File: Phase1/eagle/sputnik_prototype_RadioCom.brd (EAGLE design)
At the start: 100 x 80 mm, 74 parts, among them X2 332-22, Y1 32MHz

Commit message: fixed symbols
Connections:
- net N$20 renamed LNA_OUT
- net N$5 renamed LNA_IN
- removed net N$2 (its old number): C24.1, C43.+, L8.2, R1.2
- removed net N$9: C36.1, U$7.5
- new net VBIAS: C24.1, C36.1, C43.+, L8.2, R1.2, U$7.5

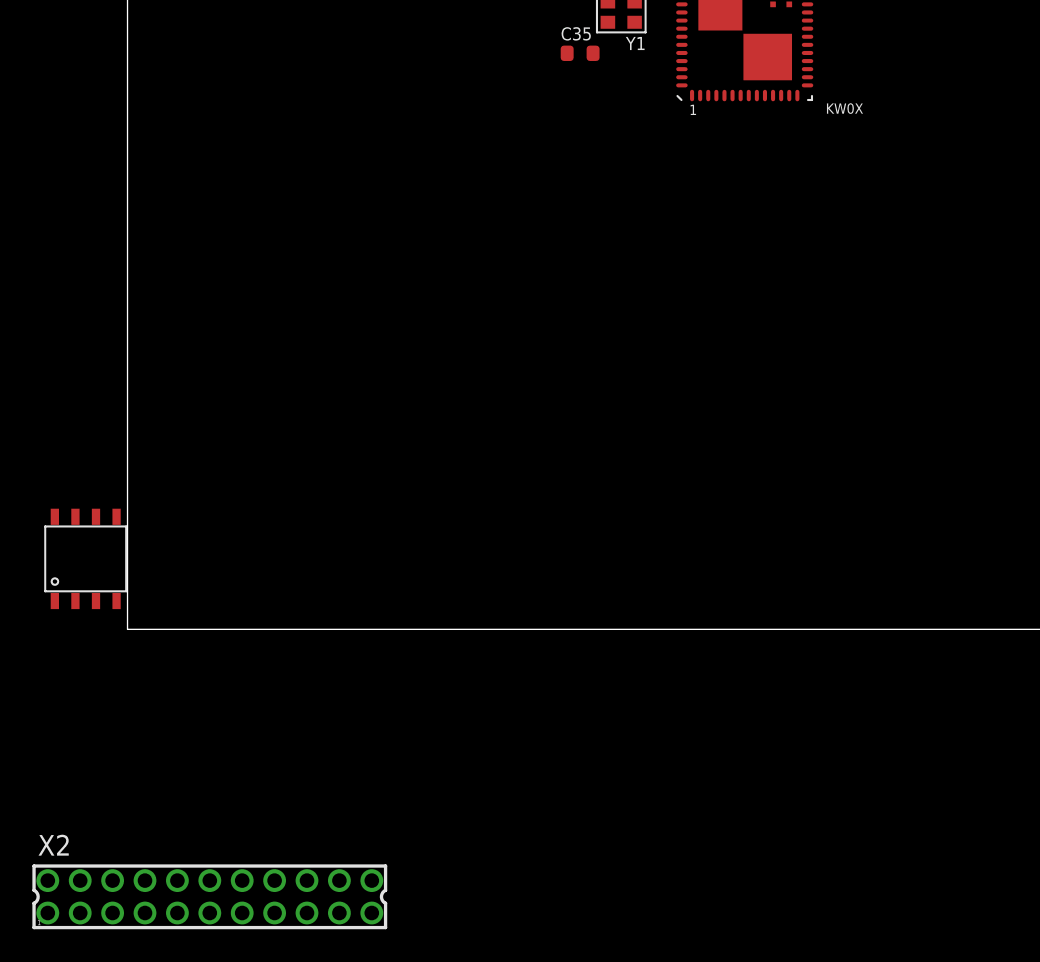
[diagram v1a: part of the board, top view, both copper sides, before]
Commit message: Added GPIO bus
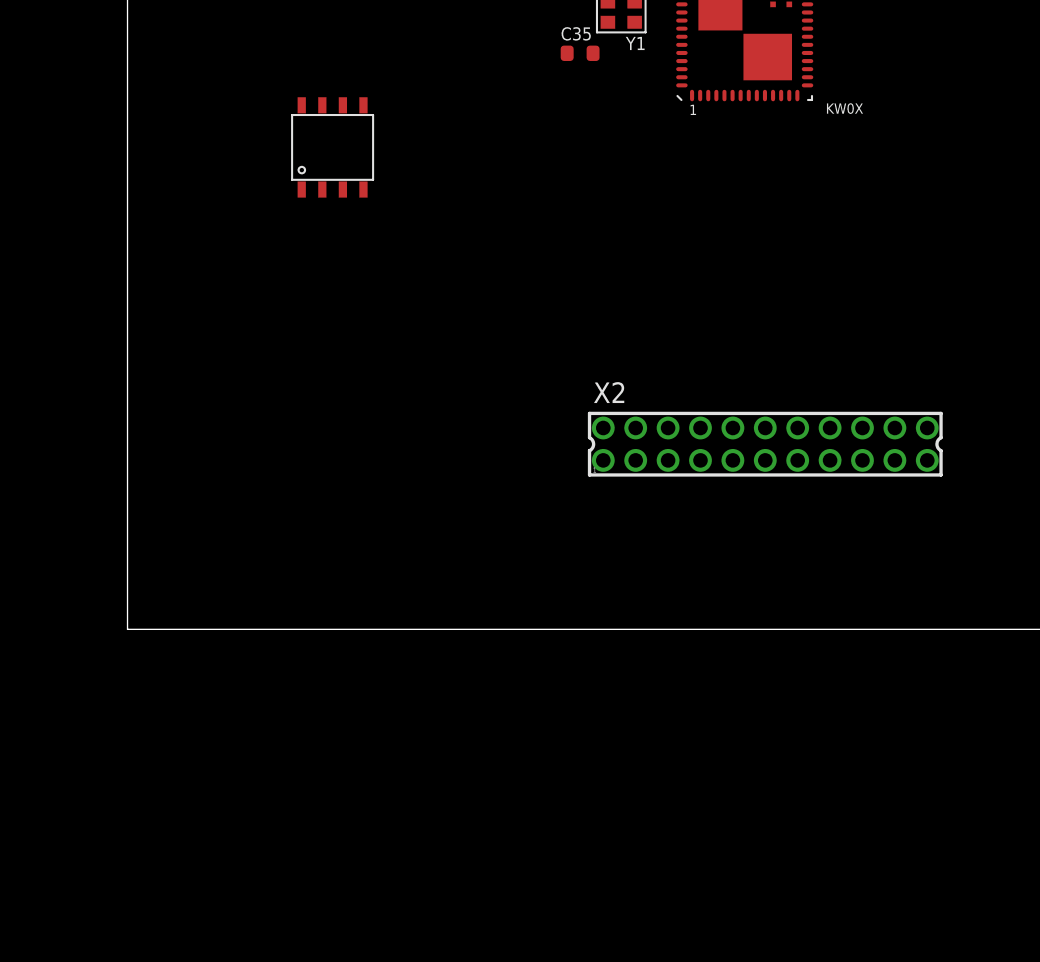
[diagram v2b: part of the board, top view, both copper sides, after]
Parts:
- moved X2 44.2 mm to (39.4, 11.4)
- moved U$1 29.6 mm to (10.2, 31.8)
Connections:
- removed net N$32: KW0X.50, X2.2
- removed net N$33: KW0X.5, X2.3
- removed net N$35: KW0X.6, X2.4
- removed net N$36: KW0X.7, X2.5
- removed net N$37: KW0X.8, X2.6
- removed net N$38: KW0X.9, X2.7
- removed net N$4: KW0X.49, X2.1
- removed net PTB0: KW0X.17
- removed net PTB1: KW0X.18, X2.12
- removed net PTB17: KW0X.22, X2.14
- removed net PTB2: KW0X.21, X2.13
- removed net PTBO: X2.11
- removed net PTC1: KW0X.24, X2.15
- removed net PTC2: KW0X.25, X2.16
- removed net PTC3: KW0X.26, X2.17
- removed net PTC4: KW0X.23, X2.18
- removed net PTC5: KW0X.59, X2.19
- removed net PTC6: KW0X.60, X2.20
- new net GPIO0: KW0X.17, X2.1
- new net GPIO1: KW0X.18, X2.2
- new net GPIO10: KW0X.49, X2.11
- new net GPIO11: KW0X.50, X2.12
- new net GPIO12: KW0X.5, X2.13
- new net GPIO13: KW0X.6, X2.14
- new net GPIO14: KW0X.7, X2.15
- new net GPIO15: KW0X.8, X2.16
- new net GPIO16: KW0X.9, X2.17
- new net GPIO2: KW0X.21, X2.3
- new net GPIO3: KW0X.22, X2.4
- new net GPIO4: KW0X.24, X2.5
- new net GPIO5: KW0X.25, X2.6
- new net GPIO6: KW0X.26, X2.7
- new net GPIO7: KW0X.23, X2.8
- new net GPIO8: KW0X.59, X2.9
- new net GPIO9: KW0X.60, X2.10
- net PE0/UART0RX: now also X2.18; no longer X2.8
- net PE1/UART0TX: now also X2.19; no longer X2.9
- net PE3: now also X2.20; no longer X2.10

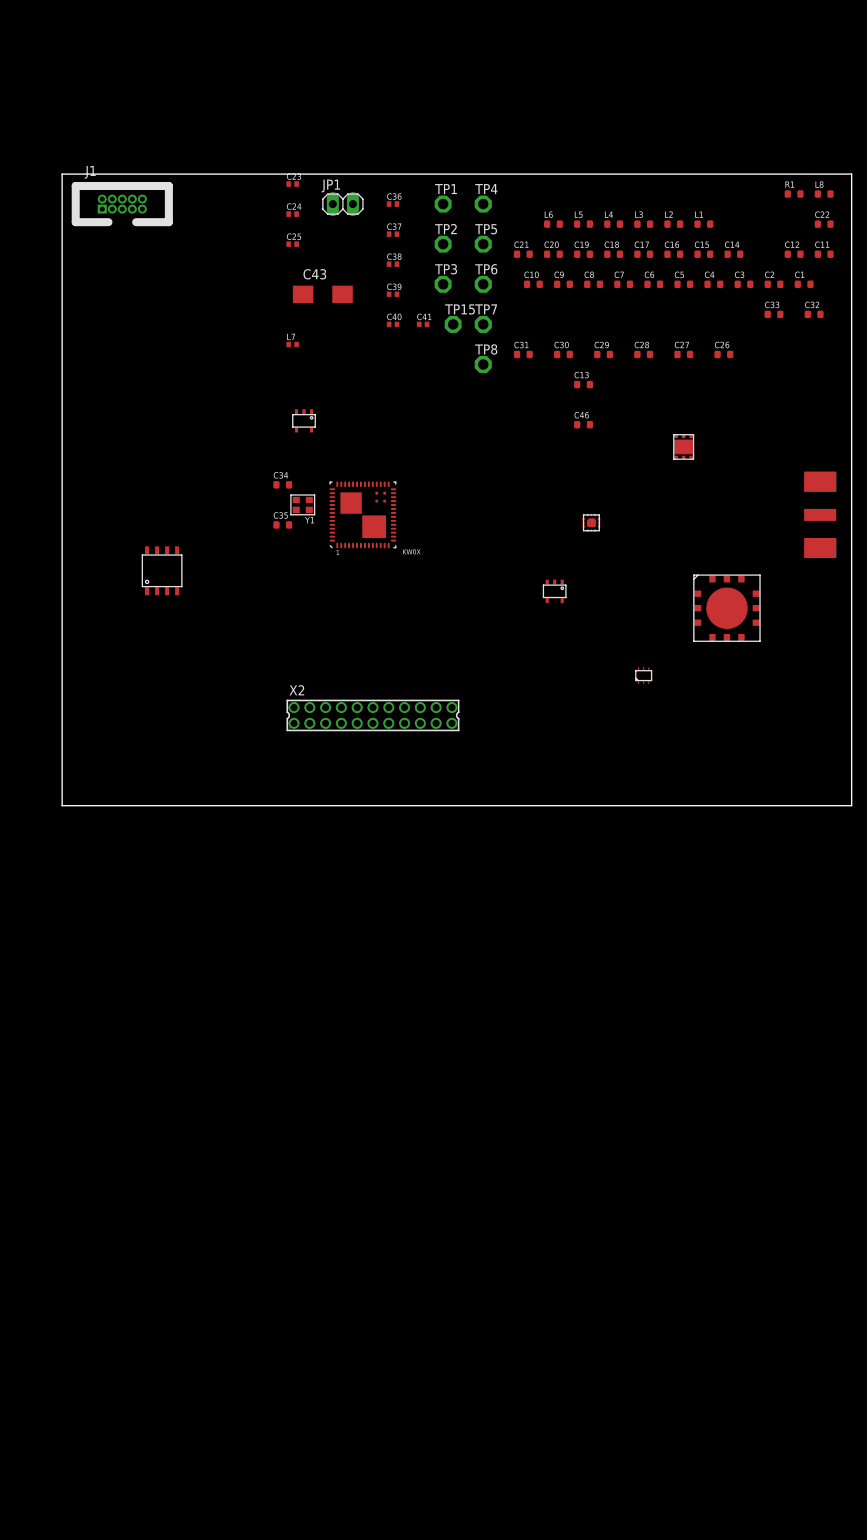
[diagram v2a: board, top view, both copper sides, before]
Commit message: Lots of OCD cleanup on schematic, bringing up to PSAS standards. Fixed lack of bypass cap on SPI flash, changed SPI flash KW0x pins to SPI1 which weren't before (?), removed DIO1 and DIO0 from GPIO bus, made debug connector, added OreSat v0.3 card outline, roughly positioned connectors, and ran and fixed ERC errors. STILL ERC ERRORS LEFT, specifically the RF_RESET or SOMETHING line. In general: nice work guys! I didn't even hate it.
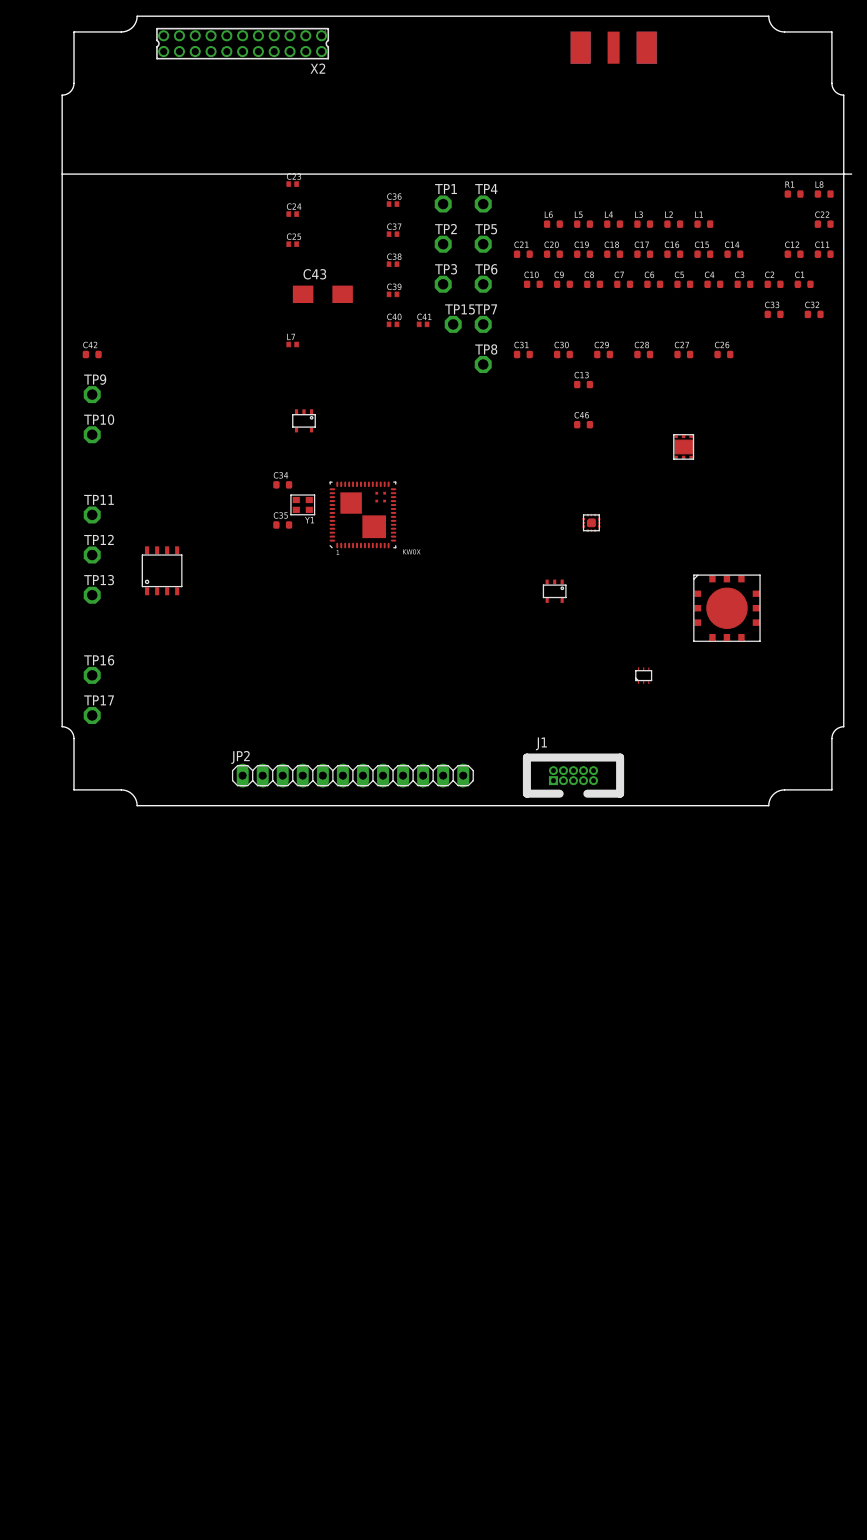
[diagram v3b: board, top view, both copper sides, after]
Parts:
- removed JP1: (no value), psas_c3_team05:1X02
- added C42: 100nF, rcl_custom:.0603-B-NOSILK
- added JP2: (no value), pinhead:1X12
- added TP10, TP11, TP12, TP13, TP16, TP17, TP9: TPSPAD1-13, testpad:P1-13
- C16, C18, C20, C21: value 0.01uF -> 10nF
- moved J1 92.2 mm to (64.8, 3.81)
- moved X2 86.7 mm to (22.9, 96.5), turned to 180 degrees
- moved SMA 65.4 mm to (69.8, 96.5), turned to 180 degrees
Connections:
- net GPIO12 renamed PTE16
- net GPIO13 renamed PTE17
- net GPIO14 renamed PTE18
- net GPIO15 renamed PTE19
- net GPIO2 renamed PTB2
- net GPIO3 renamed PTB17
- net N$29 renamed VR_PA
- net PTA0 renamed SWD_CLK
- net PTA3 renamed SWD_DIO
- removed net GPIO0: KW0X.17, X2.1
- removed net GPIO1: KW0X.18, X2.2
- removed net GPIO10: KW0X.49, X2.11
- removed net GPIO11: KW0X.50, X2.12
- removed net GPIO16: KW0X.9, X2.17
- removed net GPIO4: KW0X.24, X2.5
- removed net GPIO5: KW0X.25, X2.6
- removed net GPIO6: KW0X.26, X2.7
- removed net GPIO7: KW0X.23, X2.8
- removed net GPIO8: KW0X.59, X2.9
- removed net GPIO9: KW0X.60, X2.10
- removed net N$11: C26.1, C27.1, C28.2, C29.2, C39.1, KW0X.1, KW0X.19, KW0X.55, KW0X.56, U$8.5
- removed net N$12: KW0X.29, TP4.TP, U$1.2
- removed net N$14: KW0X.28, TP3.TP, U$1.6
- removed net N$15: KW0X.31, TP5.TP, U$1.5
- removed net N$23: KW0X.58, TP1.TP, U$1.7
- removed net N$26: KW0X.32, U$1.3
- removed net N$28: KW0X.27, TP2.TP, U$1.1
- removed net PE0/UART0RX: KW0X.13, TP7.TP, X2.18
- removed net PE1/UART0TX: KW0X.14, TP6.TP, X2.19
- removed net PE3: J1.10, KW0X.33, TP8.TP, X2.20
- removed net RF_RESET: X2.21
- new net !CS: KW0X.27, TP1.TP, U$1.1
- new net !HOLD: KW0X.32, TP10.TP, U$1.7
- new net !RESET: J1.10, KW0X.33, TP8.TP
- new net !WP: KW0X.34, TP5.TP, U$1.3
- new net DIO0: KW0X.49, TP16.TP
- new net DIO1: KW0X.50, TP17.TP
- new net MISO: KW0X.29, TP3.TP, U$1.2
- new net MOSI: KW0X.31, TP4.TP, U$1.5
- new net N$3: KW0X.51, TP11.TP
- new net N$4: TP9.TP, U$9.4
- new net N$5: KW0X.52, TP12.TP
- new net N$9: KW0X.53, TP13.TP
- new net PTC1: JP2.3, KW0X.24, X2.5
- new net PTC2: JP2.4, KW0X.25, X2.6
- new net PTC3: JP2.5, KW0X.26, X2.7
- new net PTC4: JP2.6, KW0X.23, X2.8
- new net PTC5: JP2.7, KW0X.59, X2.9
- new net PTC6: JP2.8, KW0X.60, X2.10
- new net PTC7: JP2.9, KW0X.57, X2.11
- new net PTD0: KW0X.58, X2.12
- new net PTE30: KW0X.9
- new net SCLK: KW0X.28, TP2.TP, U$1.6
- new net UART0_RX: JP2.10, KW0X.14, TP6.TP, X2.19, X2.20
- new net UART0_TX: JP2.11, KW0X.13, TP7.TP, X2.17, X2.18
- net 3.3V: now also C26.1, C27.1, C28.2, C29.2, C39.1, C42.2, JP2.2, KW0X.1, KW0X.19, KW0X.55, KW0X.56, U$1.8, U$8.5
- net GND: now also C42.1, JP2.12, X2.21, X2.22; no longer JP1.2, U$9.4
- net LNA_EN: now also KW0X.17; no longer KW0X.57
- net PA_EN: now also KW0X.18; no longer KW0X.34
- net V+: now also JP2.1, X2.1, X2.2; no longer JP1.1, U$1.8, X2.22
- net VBIAS: now also LNA.1
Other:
- board size 100 x 80 mm -> 100 x 100 mm
- board text added: "NEEDS POSITIONING"
